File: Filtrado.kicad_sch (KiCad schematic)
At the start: 31 parts

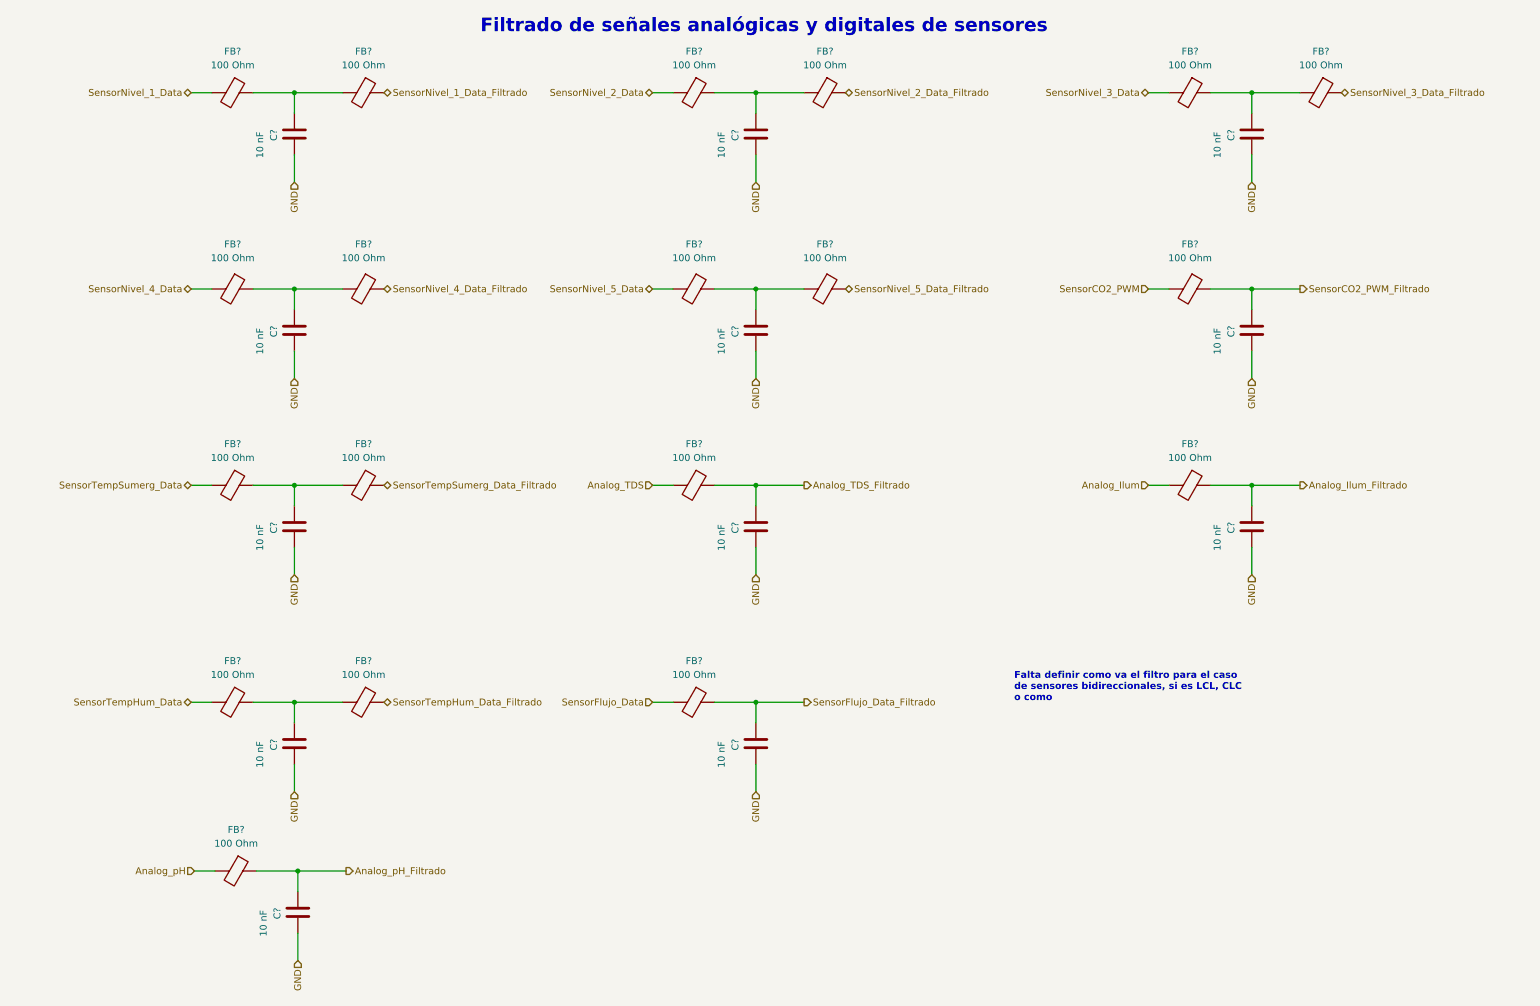
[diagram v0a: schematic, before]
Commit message: Ajuste del esquematico
Se cambio el integrado ESP32 por 2 tiras de pines de 1x15, se quitaron los switches EN y BOOT que ya estan en el NodeMCU, se quito el mutliplexor 74HC y se cablearon las I/O
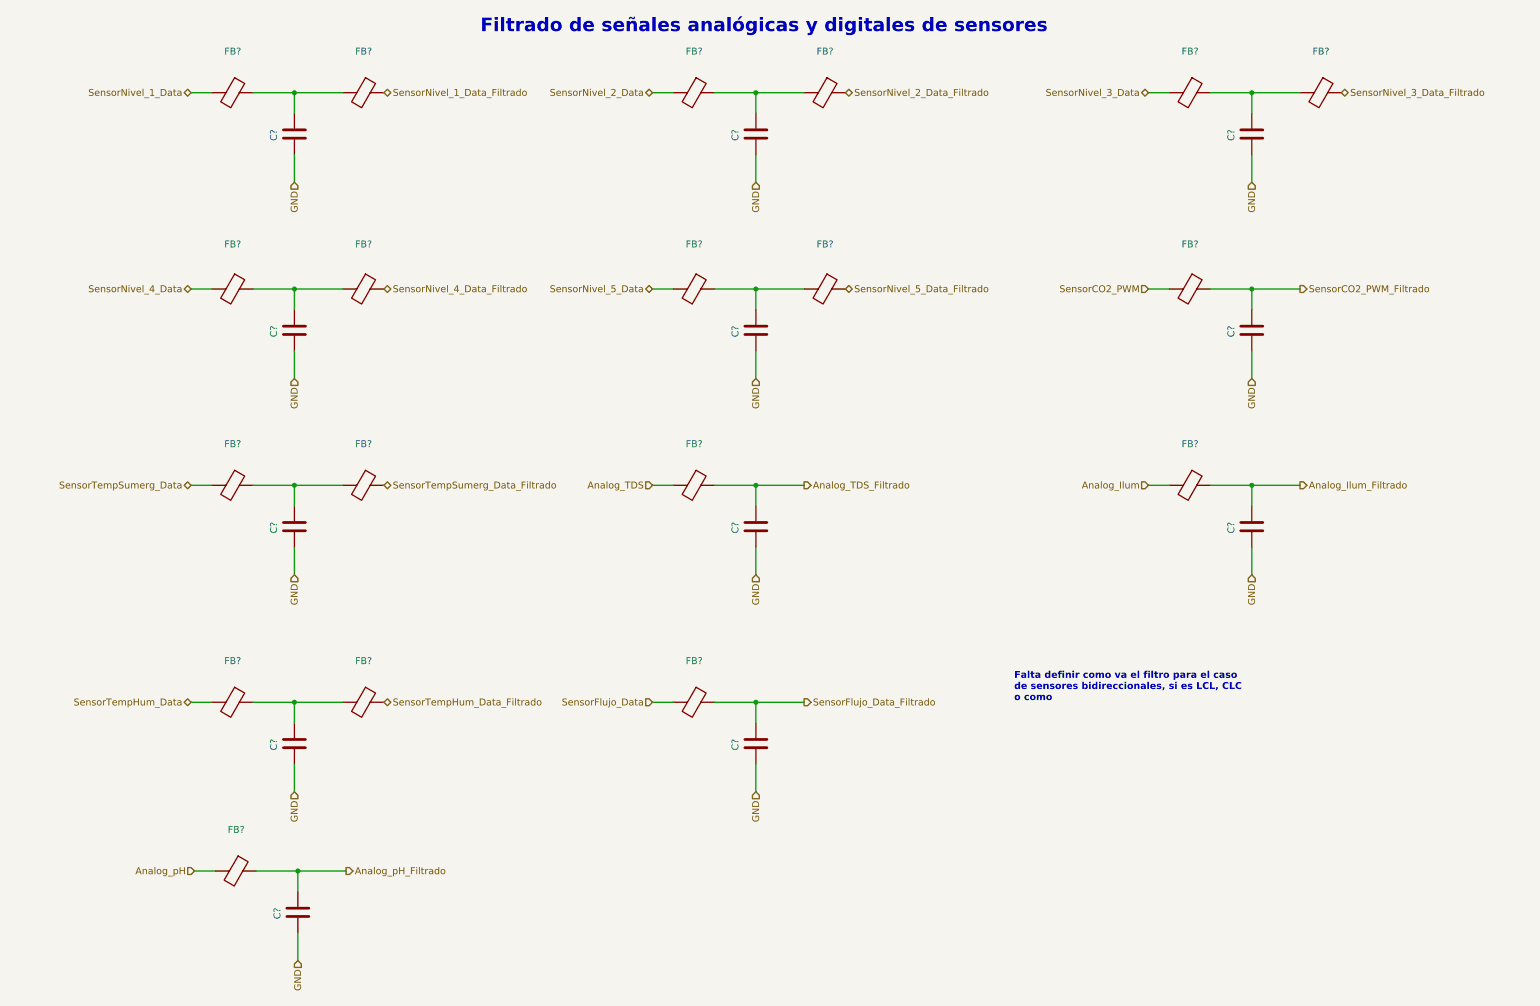
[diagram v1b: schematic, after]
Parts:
- C? (x12): value 10 nF -> (none)
- FB? (x19): value 100 Ohm -> (none)
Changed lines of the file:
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@@
     (in_bom yes) (on_board yes) (fields_autoplaced)
     (property "Reference" "FB?" (id 0) (at 251.5108 20.955 90))
-    (property "Value" "100 Ohm" (id 1) (at 251.5108 23.495 90))
+    (property "Value" "" (id 1) (at 251.5108 23.495 90))
     (property "Footprint" "" (id 2) (at 251.46 26.797 90)
       (effects (font (size 1.27 1.27)) hide)
@@
     (in_bom yes) (on_board yes) (fields_autoplaced)
     (property "Reference" "FB?" (id 0) (at 135.9408 93.345 90))
-    (property "Value" "100 Ohm" (id 1) (at 135.9408 95.885 90))
+    (property "Value" "" (id 1) (at 135.9408 95.885 90))
     (property "Footprint" "" (id 2) (at 135.89 99.187 90)
       (effects (font (size 1.27 1.27)) hide)
@@
       (effects (font (size 1.27 1.27)) (justify left))
     )
-    (property "Value" "10 nF" (id 1) (at 140.97 40.64 90)
+    (property "Value" "" (id 1) (at 140.97 40.64 90)
       (effects (font (size 1.27 1.27)) (justify left))
     )
@@
       (effects (font (size 1.27 1.27)) (justify left))
     )
-    (property "Value" "10 nF" (id 1) (at 232.41 113.03 90)
+    (property "Value" "" (id 1) (at 232.41 113.03 90)
       (effects (font (size 1.27 1.27)) (justify left))
     )
@@
       (effects (font (size 1.27 1.27)) (justify left))
     )
-    (property "Value" "10 nF" (id 1) (at 140.97 76.835 90)
+    (property "Value" "" (id 1) (at 140.97 76.835 90)
       (effects (font (size 1.27 1.27)) (justify left))
     )
@@
     (in_bom yes) (on_board yes) (fields_autoplaced)
     (property "Reference" "FB?" (id 0) (at 50.8508 56.515 90))
-    (property "Value" "100 Ohm" (id 1) (at 50.8508 59.055 90))
+    (property "Value" "" (id 1) (at 50.8508 59.055 90))
     (property "Footprint" "" (id 2) (at 50.8 62.992 90)
       (effects (font (size 1.27 1.27)) hide)
@@
       (effects (font (size 1.27 1.27)) (justify left))
     )
-    (property "Value" "10 nF" (id 1) (at 55.88 40.64 90)
+    (property "Value" "" (id 1) (at 55.88 40.64 90)
       (effects (font (size 1.27 1.27)) (justify left))
     )
@@
     (in_bom yes) (on_board yes) (fields_autoplaced)
     (property "Reference" "FB?" (id 0) (at 227.3808 56.515 90))
-    (property "Value" "100 Ohm" (id 1) (at 227.3808 59.055 90))
+    (property "Value" "" (id 1) (at 227.3808 59.055 90))
     (property "Footprint" "" (id 2) (at 227.33 62.992 90)
       (effects (font (size 1.27 1.27)) hide)
@@
       (effects (font (size 1.27 1.27)) (justify left))
     )
-    (property "Value" "10 nF" (id 1) (at 56.515 184.15 90)
+    (property "Value" "" (id 1) (at 56.515 184.15 90)
       (effects (font (size 1.27 1.27)) (justify left))
     )
@@
       (effects (font (size 1.27 1.27)) (justify left))
     )
-    (property "Value" "10 nF" (id 1) (at 232.41 76.835 90)
+    (property "Value" "" (id 1) (at 232.41 76.835 90)
       (effects (font (size 1.27 1.27)) (justify left))
     )
@@
       (effects (font (size 1.27 1.27)) (justify left))
     )
-    (property "Value" "10 nF" (id 1) (at 140.97 153.035 90)
+    (property "Value" "" (id 1) (at 140.97 153.035 90)
       (effects (font (size 1.27 1.27)) (justify left))
     )
@@
     (in_bom yes) (on_board yes) (fields_autoplaced)
     (property "Reference" "FB?" (id 0) (at 50.8508 93.345 90))
-    (property "Value" "100 Ohm" (id 1) (at 50.8508 95.885 90))
+    (property "Value" "" (id 1) (at 50.8508 95.885 90))
     (property "Footprint" "" (id 2) (at 50.8 99.187 90)
       (effects (font (size 1.27 1.27)) hide)
@@
     (in_bom yes) (on_board yes) (fields_autoplaced)
     (property "Reference" "FB?" (id 0) (at 74.9808 20.955 90))
-    (property "Value" "100 Ohm" (id 1) (at 74.9808 23.495 90))
+    (property "Value" "" (id 1) (at 74.9808 23.495 90))
     (property "Footprint" "" (id 2) (at 74.93 26.797 90)
       (effects (font (size 1.27 1.27)) hide)
@@
     (in_bom yes) (on_board yes) (fields_autoplaced)
     (property "Reference" "FB?" (id 0) (at 50.8508 133.35 90))
-    (property "Value" "100 Ohm" (id 1) (at 50.8508 135.89 90))
+    (property "Value" "" (id 1) (at 50.8508 135.89 90))
     (property "Footprint" "" (id 2) (at 50.8 139.192 90)
       (effects (font (size 1.27 1.27)) hide)
@@
       (effects (font (size 1.27 1.27)) (justify left))
     )
-    (property "Value" "10 nF" (id 1) (at 140.97 113.03 90)
+    (property "Value" "" (id 1) (at 140.97 113.03 90)
       (effects (font (size 1.27 1.27)) (justify left))
     )
@@
     (in_bom yes) (on_board yes) (fields_autoplaced)
     (property "Reference" "FB?" (id 0) (at 51.4858 164.465 90))
-    (property "Value" "100 Ohm" (id 1) (at 51.4858 167.005 90))
+    (property "Value" "" (id 1) (at 51.4858 167.005 90))
     (property "Footprint" "" (id 2) (at 51.435 170.307 90)
       (effects (font (size 1.27 1.27)) hide)
@@
       (effects (font (size 1.27 1.27)) (justify left))
     )
-    (property "Value" "10 nF" (id 1) (at 55.88 76.835 90)
+    (property "Value" "" (id 1) (at 55.88 76.835 90)
       (effects (font (size 1.27 1.27)) (justify left))
     )
@@
       (effects (font (size 1.27 1.27)) (justify left))
     )
-    (property "Value" "10 nF" (id 1) (at 232.41 40.64 90)
+    (property "Value" "" (id 1) (at 232.41 40.64 90)
       (effects (font (size 1.27 1.27)) (justify left))
     )
@@
       (effects (font (size 1.27 1.27)) (justify left))
     )
-    (property "Value" "10 nF" (id 1) (at 55.88 153.035 90)
+    (property "Value" "" (id 1) (at 55.88 153.035 90)
       (effects (font (size 1.27 1.27)) (justify left))
     )
@@
     (in_bom yes) (on_board yes) (fields_autoplaced)
     (property "Reference" "FB?" (id 0) (at 160.0708 56.515 90))
-    (property "Value" "100 Ohm" (id 1) (at 160.0708 59.055 90))
+    (property "Value" "" (id 1) (at 160.0708 59.055 90))
     (property "Footprint" "" (id 2) (at 160.02 62.992 90)
       (effects (font (size 1.27 1.27)) hide)
@@
     (in_bom yes) (on_board yes) (fields_autoplaced)
     (property "Reference" "FB?" (id 0) (at 74.9808 56.515 90))
-    (property "Value" "100 Ohm" (id 1) (at 74.9808 59.055 90))
+    (property "Value" "" (id 1) (at 74.9808 59.055 90))
     (property "Footprint" "" (id 2) (at 74.93 62.992 90)
       (effects (font (size 1.27 1.27)) hide)
@@
     (in_bom yes) (on_board yes) (fields_autoplaced)
     (property "Reference" "FB?" (id 0) (at 50.8508 20.955 90))
-    (property "Value" "100 Ohm" (id 1) (at 50.8508 23.495 90))
+    (property "Value" "" (id 1) (at 50.8508 23.495 90))
     (property "Footprint" "" (id 2) (at 50.8 26.797 90)
       (effects (font (size 1.27 1.27)) hide)
@@
     (in_bom yes) (on_board yes) (fields_autoplaced)
     (property "Reference" "FB?" (id 0) (at 135.9408 133.35 90))
-    (property "Value" "100 Ohm" (id 1) (at 135.9408 135.89 90))
+    (property "Value" "" (id 1) (at 135.9408 135.89 90))
     (property "Footprint" "" (id 2) (at 135.89 139.192 90)
       (effects (font (size 1.27 1.27)) hide)
@@
     (in_bom yes) (on_board yes) (fields_autoplaced)
     (property "Reference" "FB?" (id 0) (at 74.9808 133.35 90))
-    (property "Value" "100 Ohm" (id 1) (at 74.9808 135.89 90))
+    (property "Value" "" (id 1) (at 74.9808 135.89 90))
     (property "Footprint" "" (id 2) (at 74.93 139.192 90)
       (effects (font (size 1.27 1.27)) hide)
@@
     (in_bom yes) (on_board yes) (fields_autoplaced)
     (property "Reference" "FB?" (id 0) (at 135.9408 56.515 90))
-    (property "Value" "100 Ohm" (id 1) (at 135.9408 59.055 90))
+    (property "Value" "" (id 1) (at 135.9408 59.055 90))
     (property "Footprint" "" (id 2) (at 135.89 62.992 90)
       (effects (font (size 1.27 1.27)) hide)
@@
       (effects (font (size 1.27 1.27)) (justify left))
     )
-    (property "Value" "10 nF" (id 1) (at 55.88 113.03 90)
+    (property "Value" "" (id 1) (at 55.88 113.03 90)
       (effects (font (size 1.27 1.27)) (justify left))
     )
@@
     (in_bom yes) (on_board yes) (fields_autoplaced)
     (property "Reference" "FB?" (id 0) (at 227.3808 93.345 90))
-    (property "Value" "100 Ohm" (id 1) (at 227.3808 95.885 90))
+    (property "Value" "" (id 1) (at 227.3808 95.885 90))
     (property "Footprint" "" (id 2) (at 227.33 99.187 90)
       (effects (font (size 1.27 1.27)) hide)
@@
     (in_bom yes) (on_board yes) (fields_autoplaced)
     (property "Reference" "FB?" (id 0) (at 160.0708 20.955 90))
-    (property "Value" "100 Ohm" (id 1) (at 160.0708 23.495 90))
+    (property "Value" "" (id 1) (at 160.0708 23.495 90))
     (property "Footprint" "" (id 2) (at 160.02 26.797 90)
       (effects (font (size 1.27 1.27)) hide)
@@
     (in_bom yes) (on_board yes) (fields_autoplaced)
     (property "Reference" "FB?" (id 0) (at 74.9808 93.345 90))
-    (property "Value" "100 Ohm" (id 1) (at 74.9808 95.885 90))
+    (property "Value" "" (id 1) (at 74.9808 95.885 90))
     (property "Footprint" "" (id 2) (at 74.93 99.187 90)
       (effects (font (size 1.27 1.27)) hide)
@@
     (in_bom yes) (on_board yes) (fields_autoplaced)
     (property "Reference" "FB?" (id 0) (at 227.3808 20.955 90))
-    (property "Value" "100 Ohm" (id 1) (at 227.3808 23.495 90))
+    (property "Value" "" (id 1) (at 227.3808 23.495 90))
     (property "Footprint" "" (id 2) (at 227.33 26.797 90)
       (effects (font (size 1.27 1.27)) hide)
@@
     (in_bom yes) (on_board yes) (fields_autoplaced)
     (property "Reference" "FB?" (id 0) (at 135.9408 20.955 90))
-    (property "Value" "100 Ohm" (id 1) (at 135.9408 23.495 90))
+    (property "Value" "" (id 1) (at 135.9408 23.495 90))
     (property "Footprint" "" (id 2) (at 135.89 26.797 90)
       (effects (font (size 1.27 1.27)) hide)

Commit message: Modificación de posición de circ. filtrado y circ. de adaptación de tensión
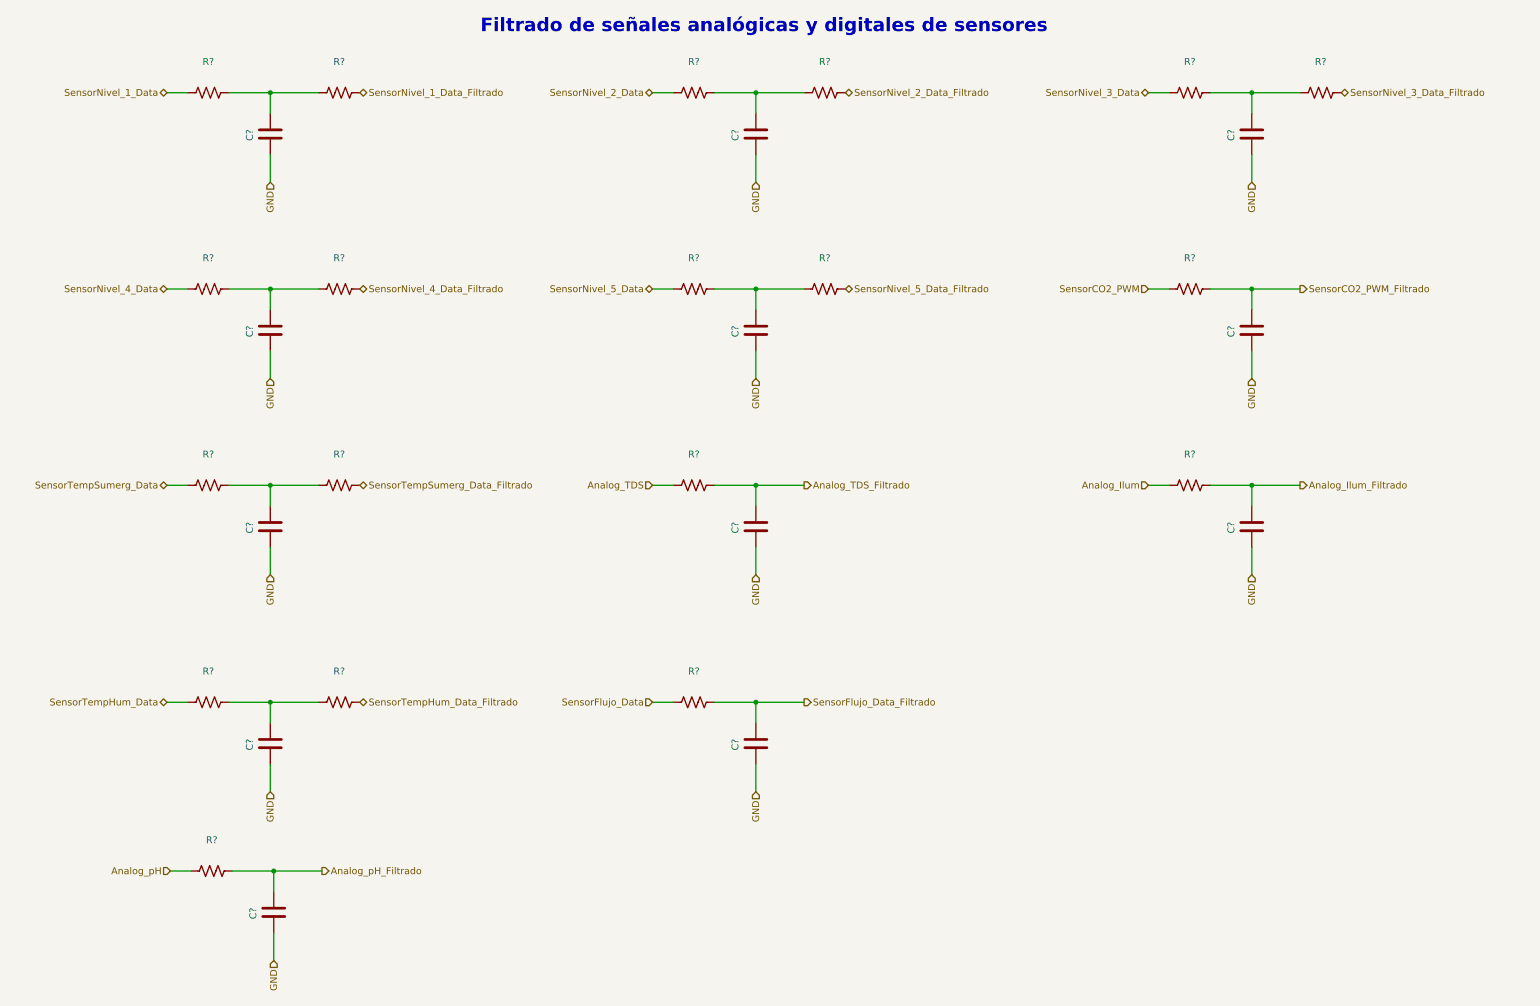
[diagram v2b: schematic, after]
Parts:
- removed C? (x11): (no value), symbol Device:C
- removed FB? (x19): (no value), symbol Device:FerriteBead
- added C? (x11): (no value), symbol Device:C
- added R? (x19): (no value), symbol Device:R_US
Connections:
- net Analog_Ilum: now also R?.1
- net Analog_Ilum_Filtrado: now also C?.1, R?.2
- net Analog_TDS: now also R?.1
- net Analog_TDS_Filtrado: now also C?.1, R?.2
- net Analog_pH: now also R?.1
- net Analog_pH_Filtrado: now also C?.1, R?.2
- net GND: now also C?.2, C?.2, C?.2, C?.2, C?.2, C?.2, C?.2, C?.2, C?.2, C?.2, C?.2
- net SensorCO2_PWM: now also R?.1
- net SensorCO2_PWM_Filtrado: now also C?.1, R?.2
- net SensorFlujo_Data: now also R?.1
- net SensorFlujo_Data_Filtrado: now also C?.1, R?.2
- net SensorNivel_1_Data: now also R?.1
- net SensorNivel_1_Data_Filtrado: now also R?.2
- net SensorNivel_2_Data: now also R?.1
- net SensorNivel_2_Data_Filtrado: now also R?.2
- net SensorNivel_3_Data: now also R?.1
- net SensorNivel_3_Data_Filtrado: now also R?.2
- net SensorNivel_4_Data: now also R?.1
- net SensorNivel_4_Data_Filtrado: now also R?.2
- net SensorNivel_5_Data: now also R?.1
- net SensorNivel_5_Data_Filtrado: now also R?.2
- net SensorTempHum_Data: now also R?.1
- net SensorTempHum_Data_Filtrado: now also R?.2
- net SensorTempSumerg_Data: now also R?.1
- net SensorTempSumerg_Data_Filtrado: now also R?.2
- net at C?.1: now also R?.1, R?.2
- new net: C?.1, R?.1, R?.2 (x6)
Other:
- note removed: "Falta definir como va el filtro para el caso de sensores bidireccionales, si es LCL, CLC o como"
- moved on the sheet: C?
